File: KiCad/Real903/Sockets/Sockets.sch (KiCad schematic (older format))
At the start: 0 parts

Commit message: New Backplanes
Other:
- note added: "DSP-BP1-6"
- note added: "DSP-BP1-[1..5]"
- note added: "DSP-BP2-[1..2]"
- note added: "DSP-BP2-[3..4]"
- note added: "DSP-BP3-2"
- note added: "Skt 1\nSkt 2\nSkt 3"
- note added: "Skt 4\nSkt 13"
- note added: "Skt 5\nSkt 11"
- note added: "Skt 6\nSkt 7\nSkt 10"
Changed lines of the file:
@@
 $EndDescr
-$Sheet
-S 3250 3200 1750 700
-U 5F2F538B
-F0 "IO" 40
-F1 "IO.sch" 40
-F2 "GND" U R 5000 3825 40
-F3 "0v" U L 3250 3275 40
-F4 "+6v" U L 3250 3350 40
-F5 "RDR-INT" U R 5000 3250 40
-F6 "PUNCH-INT" U R 5000 3300 40
-$EndSheet
 $Sheet
 S 3250 2200 1750 700
 U 5F3239EA
-F0 "TapePSUMargins" 40
-F1 "TapePSUMargins.sch" 40
-F2 "0v" U L 3250 2300 40
-F3 "On-Off-Common" U L 3250 2350 40
-F4 "On" U L 3250 2400 40
-F5 "Off" U L 3250 2450 40
-F6 "+5vDisplay" U R 5000 2275 40
-F7 "0vDisplay" U R 5000 2350 40
-F8 "Off-Light" U L 3250 2500 40
-F9 "On-Light" U L 3250 2550 40
-F10 "Auto-Start" U L 3250 2600 40
-F11 "RDR-INT" U R 5000 2850 40
-F12 "PUNCH-INT" U R 5000 2800 40
-F13 "AUT" U L 3250 2650 40
-F14 "GND" U R 5000 2450 40
-F15 "+6v" U L 3250 2700 40
-F16 "-6v" U L 3250 2750 40
+F0 "PSUMargins" 40
+F1 "PSUMargins.sch" 40
+F2 "PW[1..19]" I L 3250 2850 32
 $EndSheet
 $Sheet
@@
 F0 "Display" 40
 F1 "Display.sch" 40
-F2 "0vDisplay" U R 5000 1375 40
-F3 "+5vDisplay" U R 5000 1450 40
-F4 "GND" U R 5000 1300 40
+F2 "#I[1..4]" I R 5000 1400 32
+F3 "S[1..4]" I R 5000 1500 32
+F4 "PW[1..19]" I L 3250 1825 32
 $EndSheet
-Wire Wire Line
-	5000 1450 5100 1450
-Wire Wire Line
-	5100 1450 5100 2275
-Wire Wire Line
-	5100 2275 5000 2275
-Wire Wire Line
-	5000 2350 5125 2350
-Wire Wire Line
-	5125 2350 5125 1375
-Wire Wire Line
-	5125 1375 5000 1375
+Text Notes 3975 1525 0    40   ~ 0
+Skt 1\nSkt 2\nSkt 3
+Text Notes 3975 2500 0    40   ~ 0
+Skt 6\nSkt 7\nSkt 10
+Text Notes 3975 3350 0    40   ~ 0
+Skt 4\nSkt 13
+Text Notes 3975 4375 0    40   ~ 0
+Skt 5\nSkt 11
+Wire Bus Line
+	5000 1400 6025 1400
+Wire Bus Line
+	6025 1400 6025 4750
+Wire Bus Line
+	6025 4750 5000 4750
+$Sheet
+S 3250 3200 1750 700
+U 5F2F538B
+F0 "IO" 40
+F1 "IO.sch" 40
+F2 "S[1..4]" I R 5000 3400 32
+F3 "PW[1..19]" I L 3250 3850 32
+F4 "AUDIO-32-14" I R 5000 3825 32
+F5 "AUT" U R 5000 3575 32
+$EndSheet
+Wire Bus Line
+	5625 3400 5625 1500
+Wire Bus Line
+	5625 1500 5000 1500
+Wire Bus Line
+	5000 3400 5625 3400
+Wire Bus Line
+	3250 1825 2950 1825
+Wire Bus Line
+	2950 1825 2950 2850
+Wire Bus Line
+	2950 2850 3250 2850
+Wire Bus Line
+	2950 3850 3250 3850
+Wire Bus Line
+	2950 2850 2950 3850
+Connection ~ 2950 2850
 $Sheet
 S 3250 4200 1750 700
@@
 F0 "Control Unit" 40
 F1 "Contol Unit.sch" 40
-F2 "GND" U R 5000 4350 40
-F3 "On" U L 3250 4725 40
-F4 "On-Off-Common" U L 3250 4775 40
-F5 "Off" U L 3250 4675 40
-F6 "-6v" U L 3250 4375 40
-F7 "+6v" U L 3250 4425 40
-F8 "0v" U L 3250 4825 40
-F9 "Off-Light" U L 3250 4625 40
-F10 "On-Light" U L 3250 4575 40
-F11 "AUT" U L 3250 4475 40
-F12 "Auto-Start" U L 3250 4525 40
+F2 "PW[1..19]" U L 3250 4475 32
+F3 "#I[1..4]" I R 5000 4750 32
+F4 "AUT" U R 5000 4650 32
+F5 "AUDIO-32-14" I R 5000 4275 32
 $EndSheet
-Text GLabel 5200 1300 2    40   UnSpc ~ 0
-GND
+Wire Bus Line
+	2950 3850 2950 4475
+Wire Bus Line
+	2950 4475 3250 4475
+Connection ~ 2950 3850
 Wire Wire Line
-	5200 1300 5000 1300
+	5000 3575 5300 3575
 Wire Wire Line
-	3250 4825 2775 4825
+	5300 3575 5300 4650
 Wire Wire Line
-	2775 4825 2775 3275
+	5300 4650 5000 4650
+Text Notes 3325 1275 0    32   ~ 0
+DSP-BP1-[1..5]
+Text Notes 3325 4275 0    32   ~ 0
+DSP-BP1-6
+Text Notes 3325 1350 0    32   ~ 0
+DSP-BP2-[1..2]
+Text Notes 3325 4325 0    32   ~ 0
+DSP-BP2-[3..4]
+Text Notes 3325 4375 0    32   ~ 0
+DSP-BP3-2
 Wire Wire Line
-	2775 2300 3250 2300
+	5000 4275 5125 4275
 Wire Wire Line
-	3250 2350 2800 2350
+	5125 4275 5125 3825
 Wire Wire Line
-	2800 2350 2800 4775
-Wire Wire Line
-	2800 4775 3250 4775
-Wire Wire Line
-	3250 4725 2825 4725
-Wire Wire Line
-	2825 4725 2825 2400
-Wire Wire Line
-	2825 2400 3250 2400
-Wire Wire Line
-	3250 4675 2850 4675
-Wire Wire Line
-	2850 4675 2850 2450
-Wire Wire Line
-	2850 2450 3250 2450
-Wire Wire Line
-	2875 4625 2875 2500
-Wire Wire Line
-	2875 2500 3250 2500
-Wire Wire Line
-	2875 4625 3250 4625
-Wire Wire Line
-	3250 2550 2900 2550
-Wire Wire Line
-	2900 2550 2900 4575
-Wire Wire Line
-	2900 4575 3250 4575
-Wire Wire Line
-	3250 2600 2925 2600
-Wire Wire Line
-	2925 2600 2925 4525
-Wire Wire Line
-	2925 4525 3250 4525
-Wire Wire Line
-	3250 4475 2950 4475
-Wire Wire Line
-	2950 4475 2950 2650
-Wire Wire Line
-	2950 2650 3250 2650
-Wire Wire Line
-	5000 2850 5100 2850
-Wire Wire Line
-	5100 2850 5100 3250
-Wire Wire Line
-	5100 3250 5000 3250
-Wire Wire Line
-	5000 3300 5125 3300
-Wire Wire Line
-	5125 3300 5125 2800
-Wire Wire Line
-	5125 2800 5000 2800
-Text GLabel 5200 2450 2    40   UnSpc ~ 0
-GND
-Wire Wire Line
-	5200 2450 5000 2450
-Text GLabel 5200 3825 2    40   UnSpc ~ 0
-GND
-Wire Wire Line
-	5200 3825 5000 3825
-Text GLabel 5200 4350 2    40   UnSpc ~ 0
-GND
-Wire Wire Line
-	5200 4350 5000 4350
-Wire Wire Line
-	3250 3275 2775 3275
-Connection ~ 2775 3275
-Wire Wire Line
-	2775 3275 2775 2300
-Wire Wire Line
-	3250 4425 2975 4425
-Wire Wire Line
-	2975 4425 2975 3350
-Wire Wire Line
-	2975 2700 3250 2700
-Wire Wire Line
-	3250 3350 2975 3350
-Connection ~ 2975 3350
-Wire Wire Line
-	2975 3350 2975 2700
-Wire Wire Line
-	3250 2750 3000 2750
-Wire Wire Line
-	3000 2750 3000 4375
-Wire Wire Line
-	3000 4375 3250 4375
+	5125 3825 5000 3825
 $EndSCHEMATC

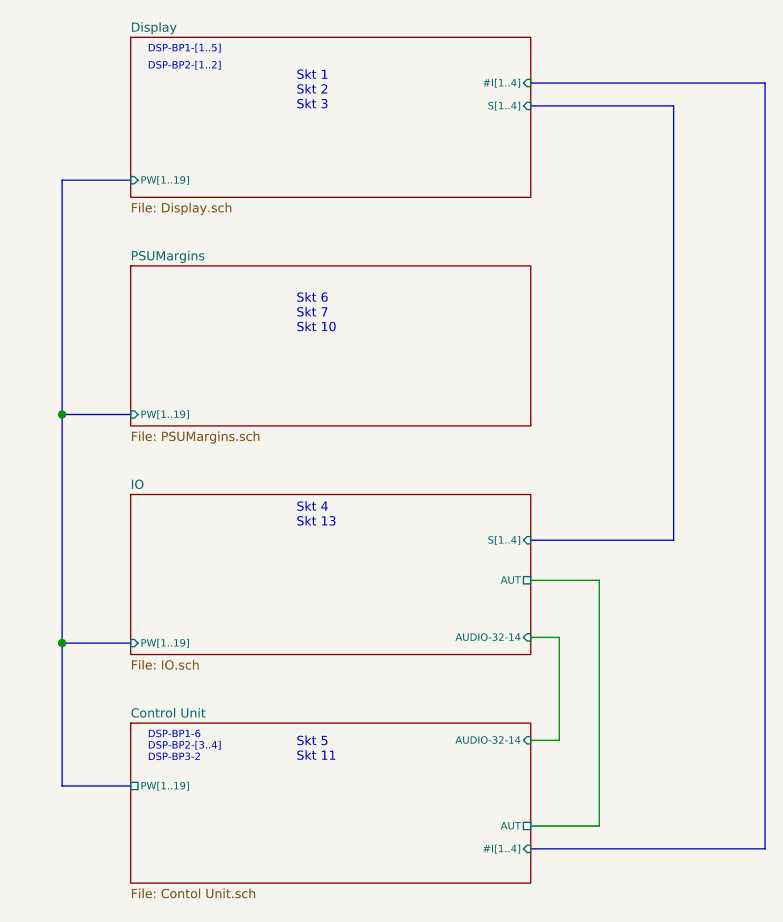
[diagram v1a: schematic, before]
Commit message: New Sockets
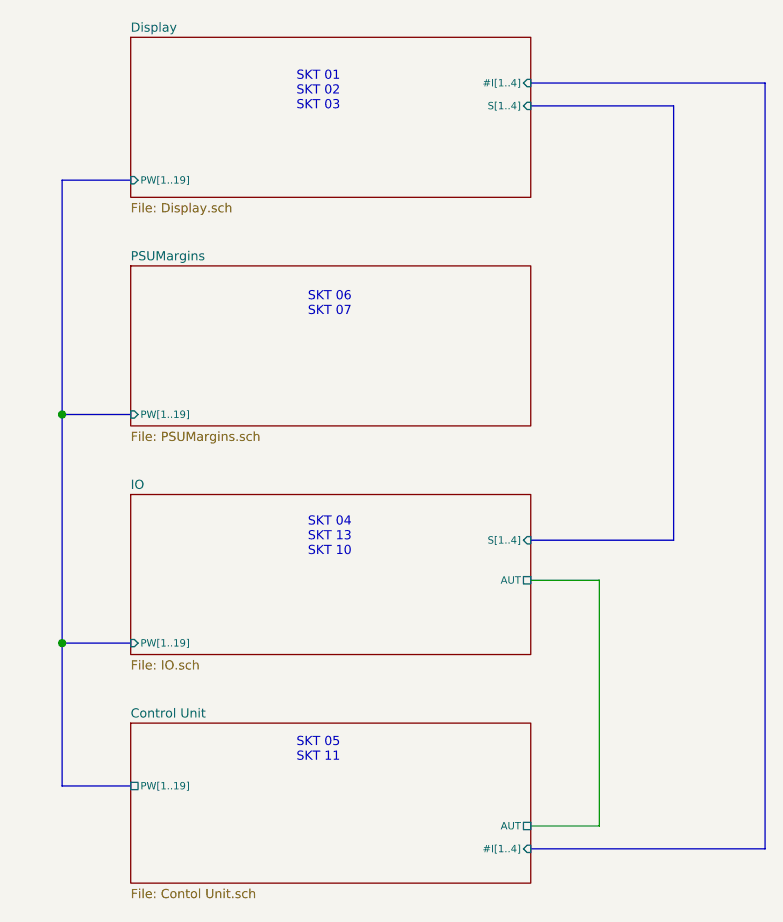
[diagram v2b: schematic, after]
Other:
- note added: "SKT 01\nSKT 02\nSKT 03"
- note added: "SKT 04\nSKT 13\nSKT 10"
- note added: "SKT 05\nSKT 11"
- note added: "SKT 06\nSKT 07"
- note removed: "DSP-BP1-6"
- note removed: "DSP-BP1-[1..5]"
- note removed: "DSP-BP2-[1..2]"
- note removed: "DSP-BP2-[3..4]"
- note removed: "DSP-BP3-2"
- note removed: "Skt 1\nSkt 2\nSkt 3"
- note removed: "Skt 4\nSkt 13"
- note removed: "Skt 5\nSkt 11"
- note removed: "Skt 6\nSkt 7\nSkt 10"
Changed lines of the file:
@@
 encoding utf-8
 Sheet 1 5
-Title ""
-Date ""
+Title "Sockets"
+Date "2023-02-11"
 Rev ""
 Comp ""
@@
 F2 "PW[1..19]" I L 3250 2850 32
 $EndSheet
-$Sheet
-S 3250 1200 1750 700
-U 5F307B10
-F0 "Display" 40
-F1 "Display.sch" 40
-F2 "#I[1..4]" I R 5000 1400 32
-F3 "S[1..4]" I R 5000 1500 32
-F4 "PW[1..19]" I L 3250 1825 32
-$EndSheet
 Text Notes 3975 1525 0    40   ~ 0
-Skt 1\nSkt 2\nSkt 3
-Text Notes 3975 2500 0    40   ~ 0
-Skt 6\nSkt 7\nSkt 10
-Text Notes 3975 3350 0    40   ~ 0
-Skt 4\nSkt 13
+SKT 01\nSKT 02\nSKT 03
+Text Notes 4025 2425 0    40   ~ 0
+SKT 06\nSKT 07
+Text Notes 4025 3475 0    40   ~ 0
+SKT 04\nSKT 13\nSKT 10
 Text Notes 3975 4375 0    40   ~ 0
-Skt 5\nSkt 11
+SKT 05\nSKT 11
 Wire Bus Line
 	5000 1400 6025 1400
@@
 F2 "S[1..4]" I R 5000 3400 32
 F3 "PW[1..19]" I L 3250 3850 32
-F4 "AUDIO-32-14" I R 5000 3825 32
-F5 "AUT" U R 5000 3575 32
+F4 "AUT" U R 5000 3575 32
 $EndSheet
 Wire Bus Line
@@
 F3 "#I[1..4]" I R 5000 4750 32
 F4 "AUT" U R 5000 4650 32
-F5 "AUDIO-32-14" I R 5000 4275 32
 $EndSheet
 Wire Bus Line
@@
 Wire Wire Line
 	5300 4650 5000 4650
-Text Notes 3325 1275 0    32   ~ 0
-DSP-BP1-[1..5]
-Text Notes 3325 4275 0    32   ~ 0
-DSP-BP1-6
-Text Notes 3325 1350 0    32   ~ 0
-DSP-BP2-[1..2]
-Text Notes 3325 4325 0    32   ~ 0
-DSP-BP2-[3..4]
-Text Notes 3325 4375 0    32   ~ 0
-DSP-BP3-2
-Wire Wire Line
-	5000 4275 5125 4275
-Wire Wire Line
-	5125 4275 5125 3825
-Wire Wire Line
-	5125 3825 5000 3825
+$Sheet
+S 3250 1200 1750 700
+U 5F307B10
+F0 "Display" 40
+F1 "Display.sch" 40
+F2 "#I[1..4]" I R 5000 1400 32
+F3 "S[1..4]" I R 5000 1500 32
+F4 "PW[1..19]" I L 3250 1825 32
+$EndSheet
 $EndSCHEMATC
